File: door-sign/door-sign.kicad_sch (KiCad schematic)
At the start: 7 parts, among them SW1 200MSP1T1B1M2QEH

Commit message: done
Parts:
- added H1, H2, H3, H4: MountingHole, parts:MountingHole_5mm, symbol parts:MountingHole
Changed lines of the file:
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@@
+    )
+  )
+  (symbol (lib_id "parts:MountingHole") (at 71.12 118.11 0) (unit 1)
+    (in_bom yes) (on_board yes) (dnp no) (fields_autoplaced)
+    (property "Reference" "H2" (at 73.66 116.84 0)
+      (effects (font (size 1.27 1.27)) (justify left))
+    )
+    (property "Value" "MountingHole" (at 73.66 119.38 0)
+      (effects (font (size 1.27 1.27)) (justify left))
+    )
+    (property "Footprint" "parts:MountingHole_5mm" (at 71.12 118.11 0)
+      (effects (font (size 1.27 1.27)) hide)
+    )
+    (property "Datasheet" "~" (at 71.12 118.11 0)
+      (effects (font (size 1.27 1.27)) hide)
+    )
+    (instances
+      (project "door-sign"
+        (path "/e88230cd-1344-4912-a3f5-29dd194fcb16"
+          (reference "H2") (unit 1)
+        )
+      )
     )
   )
@@
         )
       )
+    )
+  )
+  (symbol (lib_id "parts:MountingHole") (at 92.71 118.11 0) (unit 1)
+    (in_bom yes) (on_board yes) (dnp no) (fields_autoplaced)
+    (property "Reference" "H4" (at 95.25 116.84 0)
+      (effects (font (size 1.27 1.27)) (justify left))
+    )
+    (property "Value" "MountingHole" (at 95.25 119.38 0)
+      (effects (font (size 1.27 1.27)) (justify left))
+    )
+    (property "Footprint" "parts:MountingHole_5mm" (at 92.71 118.11 0)
+      (effects (font (size 1.27 1.27)) hide)
+    )
+    (property "Datasheet" "~" (at 92.71 118.11 0)
+      (effects (font (size 1.27 1.27)) hide)
+    )
+    (instances
+      (project "door-sign"
+        (path "/e88230cd-1344-4912-a3f5-29dd194fcb16"
+          (reference "H4") (unit 1)
+        )
+      )
+    )
+  )
+  (symbol (lib_id "parts:MountingHole") (at 71.12 111.76 0) (unit 1)
+    (in_bom yes) (on_board yes) (dnp no) (fields_autoplaced)
+    (property "Reference" "H1" (at 73.66 110.49 0)
+      (effects (font (size 1.27 1.27)) (justify left))
+    )
+    (property "Value" "MountingHole" (at 73.66 113.03 0)
+      (effects (font (size 1.27 1.27)) (justify left))
+    )
+    (property "Footprint" "parts:MountingHole_5mm" (at 71.12 111.76 0)
+      (effects (font (size 1.27 1.27)) hide)
+    )
+    (property "Datasheet" "~" (at 71.12 111.76 0)
+      (effects (font (size 1.27 1.27)) hide)
+    )
+    (instances
+      (project "door-sign"
+        (path "/e88230cd-1344-4912-a3f5-29dd194fcb16"
+          (reference "H1") (unit 1)
+        )
+      )
+    )
+  )
+  (symbol (lib_id "parts:MountingHole") (at 92.71 111.76 0) (unit 1)
+    (in_bom yes) (on_board yes) (dnp no) (fields_autoplaced)
+    (property "Reference" "H3" (at 95.25 110.49 0)
+      (effects (font (size 1.27 1.27)) (justify left))
+    )
+    (property "Value" "MountingHole" (at 95.25 113.03 0)
+      (effects (font (size 1.27 1.27)) (justify left))
+    )
+    (property "Footprint" "parts:MountingHole_5mm" (at 92.71 111.76 0)
+      (effects (font (size 1.27 1.27)) hide)
+    )
+    (property "Datasheet" "~" (at 92.71 111.76 0)
+      (effects (font (size 1.27 1.27)) hide)
+    )
+    (instances
+      (project "door-sign"
+        (path "/e88230cd-1344-4912-a3f5-29dd194fcb16"
+          (reference "H3") (unit 1)
+        )
+      )

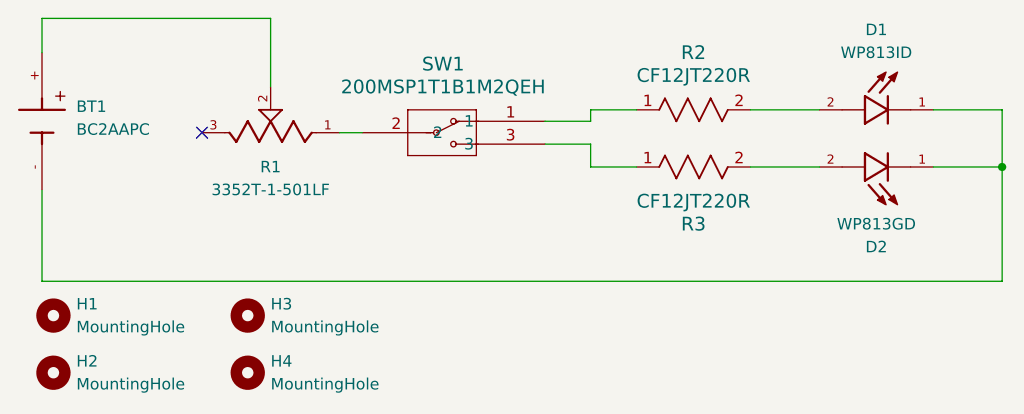
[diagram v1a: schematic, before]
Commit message: update component values
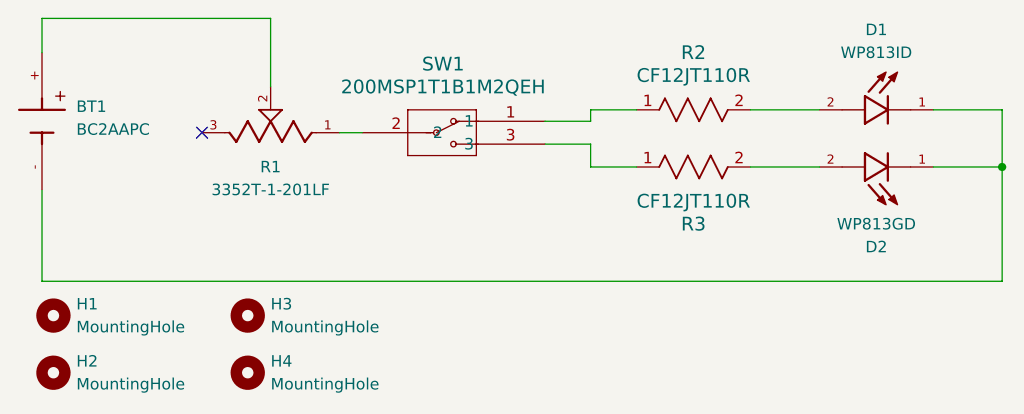
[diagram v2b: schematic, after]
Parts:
- R1: value 3352T-1-501LF -> 3352T-1-201LF
- R2, R3: value CF12JT220R -> CF12JT110R
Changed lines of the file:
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@@
       (effects (font (size 1.524 1.524)))
     )
-    (property "Value" "CF12JT220R" (at 142.24 85.09 0)
+    (property "Value" "CF12JT110R" (at 142.24 85.09 0)
       (effects (font (size 1.524 1.524)))
     )
@@
       (effects (font (size 1.27 1.27)))
     )
-    (property "Value" "3352T-1-501LF" (at 95.25 97.79 0)
+    (property "Value" "3352T-1-201LF" (at 95.25 97.79 0)
       (effects (font (size 1.27 1.27)))
     )
@@
       (effects (font (size 1.524 1.524)))
     )
-    (property "Value" "CF12JT220R" (at 142.24 99.06 0)
+    (property "Value" "CF12JT110R" (at 142.24 99.06 0)
       (effects (font (size 1.524 1.524)))
     )

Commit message: fixed errors
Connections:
- net at R2.1: now also SW1.3; no longer SW1.1
- net at R3.1: now also SW1.1; no longer SW1.3
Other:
- moved on the sheet: D1, D2, R2, R3
